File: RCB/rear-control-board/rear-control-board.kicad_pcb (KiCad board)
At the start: 2 copper layers, 99.1 x 99.1 mm, 57 parts, among them J1 Conn_01x23, J2 Conn_01x14, J3 Conn_01x08, J4 Conn_01x02, J5 Conn_01x02, J6 Conn_01x05, K1 T9VV1K15-12S, K2 G5V-2, K3 G5V-2, Q1 BSS84, Q2 2N7002, Q3 Q_PMOS_GDSD, Q4 Q_PMOS_GDSD, Q5 Q_PMOS_GDSD, U1 STM32F413CGUx, U2 LD1117S33TR_SOT223, U3 R-78B5.0-2.0, U4 MCP2551-I-SN, Y1 Crystal

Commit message: DRC and layout update
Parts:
- added G***: LOGO, AERO_Footprints:AERO_Logo_10x4mm, F.Cu at (131.5, 135.3)
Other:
- board text added: "BMS"
- board text added: "DCDC"
- board text added: "G.Spearing 22.032"
- board text added: "HVB"
- board text added: "IMD"
- board text added: "M3 Holes"
- board text added: "Pump"
- board text added: "RCB"
- board text added: "Rinehart"
- board text added: "SSOK"
- board text added: "Spare"

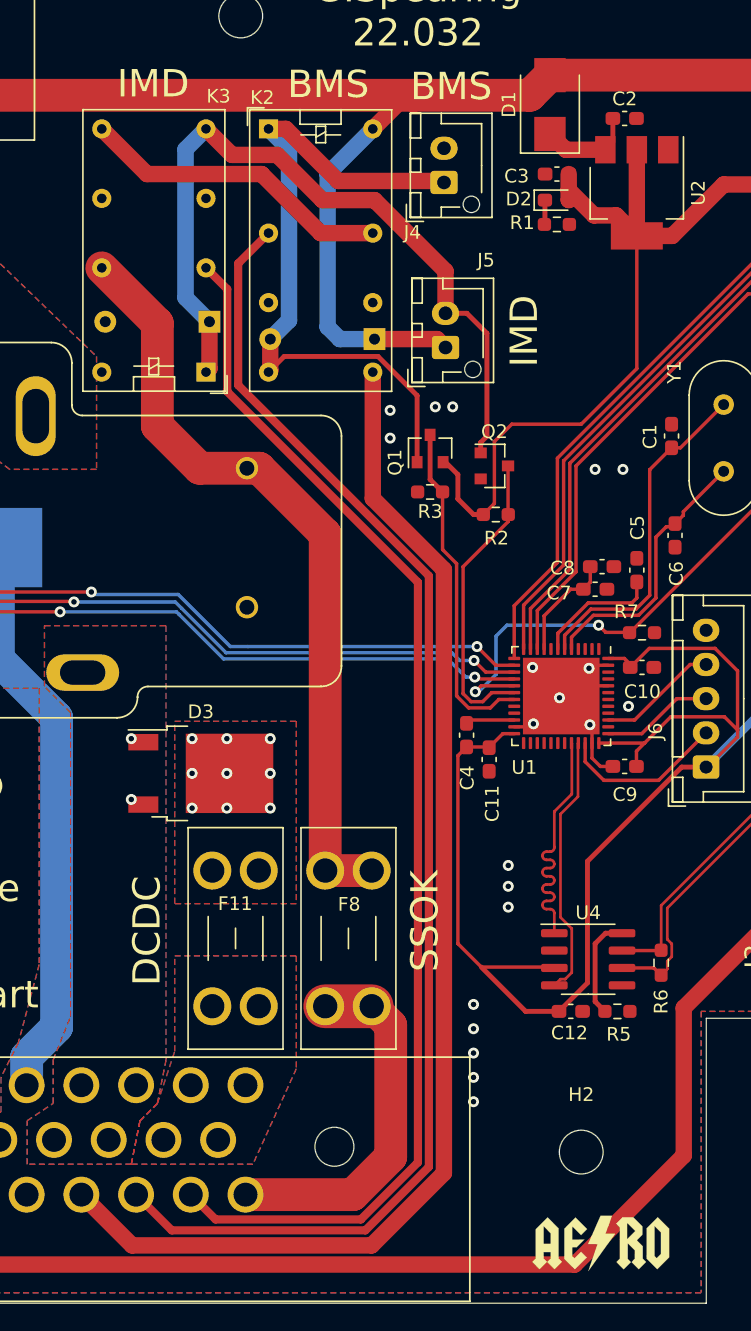
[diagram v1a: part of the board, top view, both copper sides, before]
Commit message: updating footprint and 3d model links
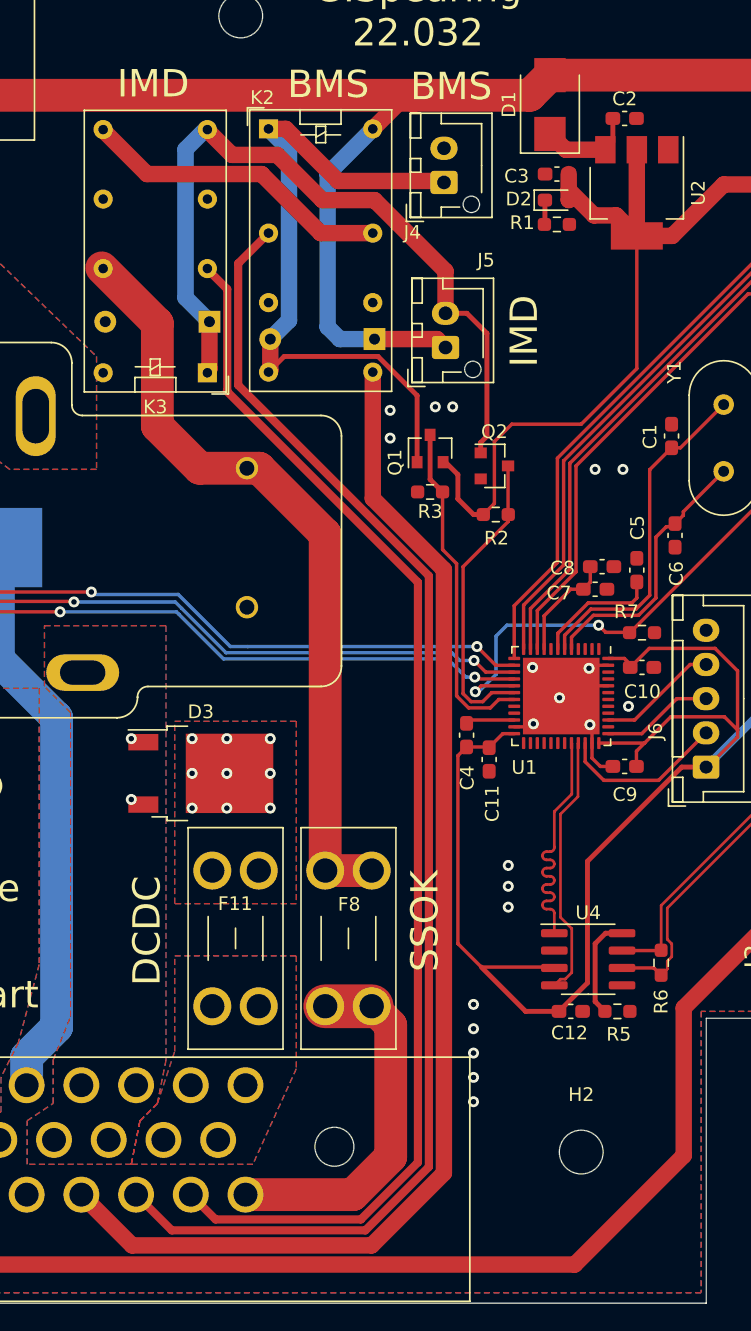
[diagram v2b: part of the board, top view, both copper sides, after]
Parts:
- removed G***: LOGO, AERO_Footprints:AERO_Logo_10x4mm
- moved K3 0.11 mm to (102.7, 71.7)

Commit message: update layout and labeling
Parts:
- moved J2 0.09 mm to (150.9, 58.0)
- moved J1 0.07 mm to (77.5, 123.7)
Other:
- board text added: "3.3V"
- board text added: "CLK"
- board text added: "DIO"
- board text added: "GND"
- board text added: "Trace"

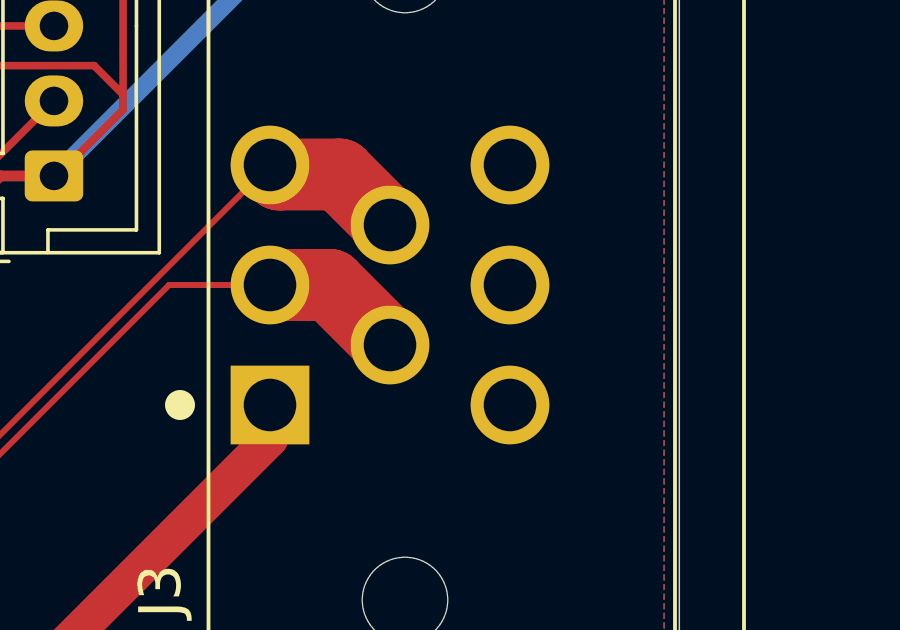
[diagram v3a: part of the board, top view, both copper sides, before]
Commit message: updating can pinouts
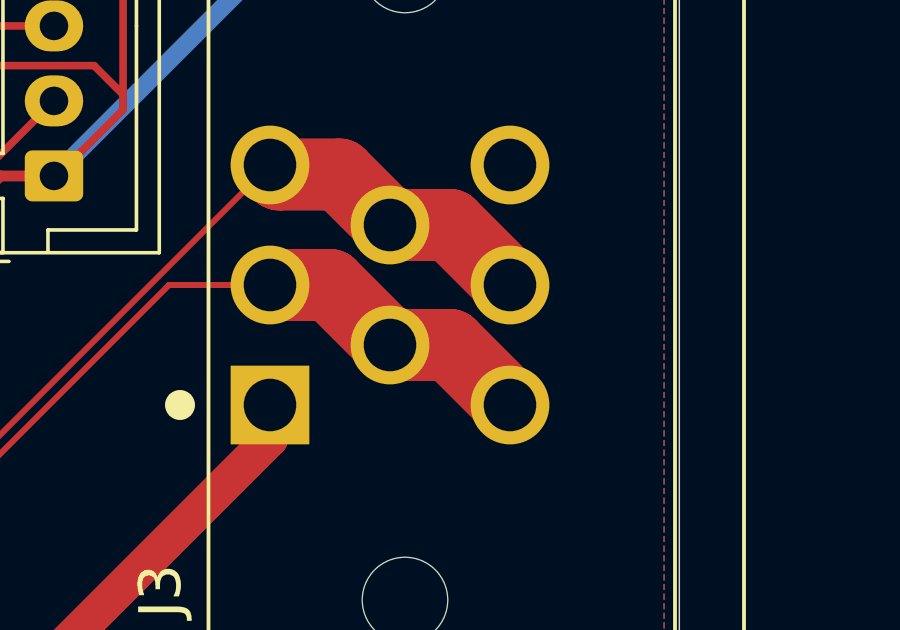
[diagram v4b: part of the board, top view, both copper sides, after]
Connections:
- J3 pad 6: /NC -> /CAN_N
- J3 pad 7: GND -> /CAN_P
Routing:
- net /CAN_P: track 25.8 -> 30.6 mm
- net /CAN_N: track 26.1 -> 30.9 mm

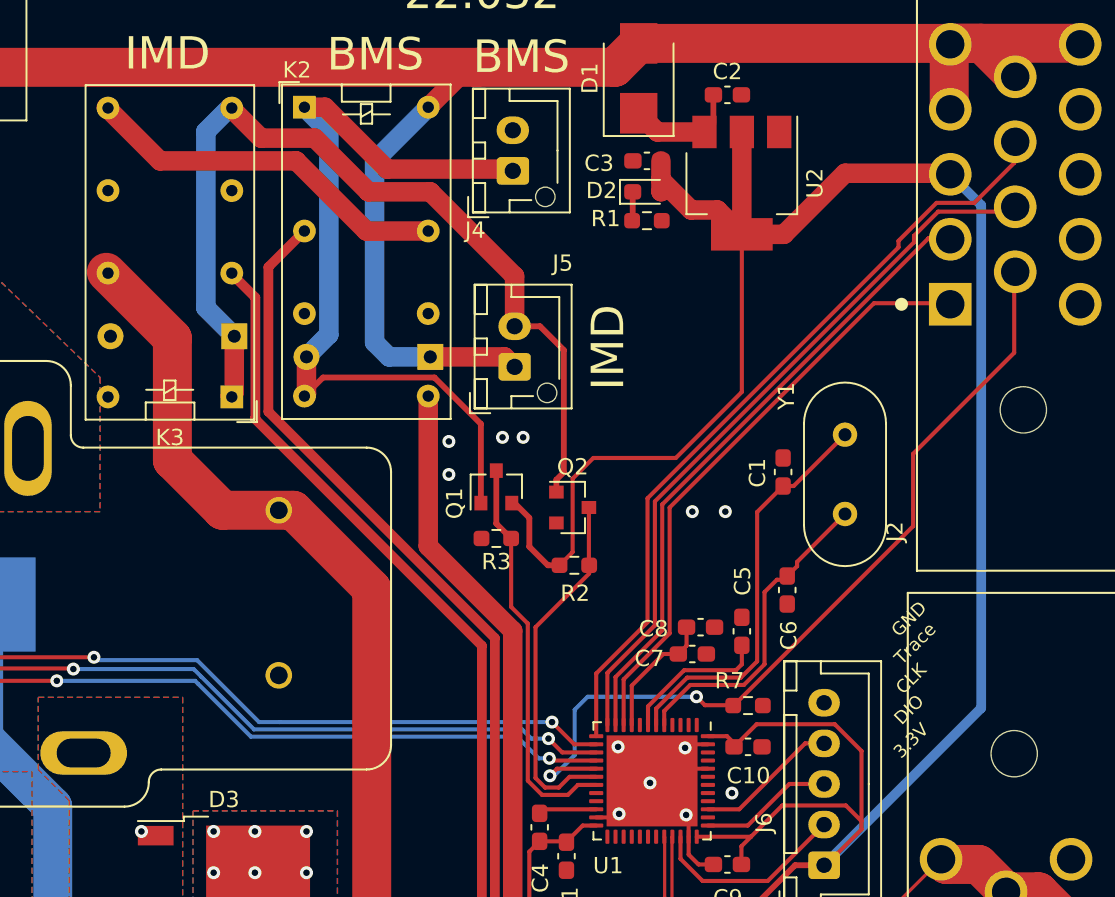
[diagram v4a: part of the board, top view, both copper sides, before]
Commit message: Major Review and Part Update
updating footprints, component values, layouts
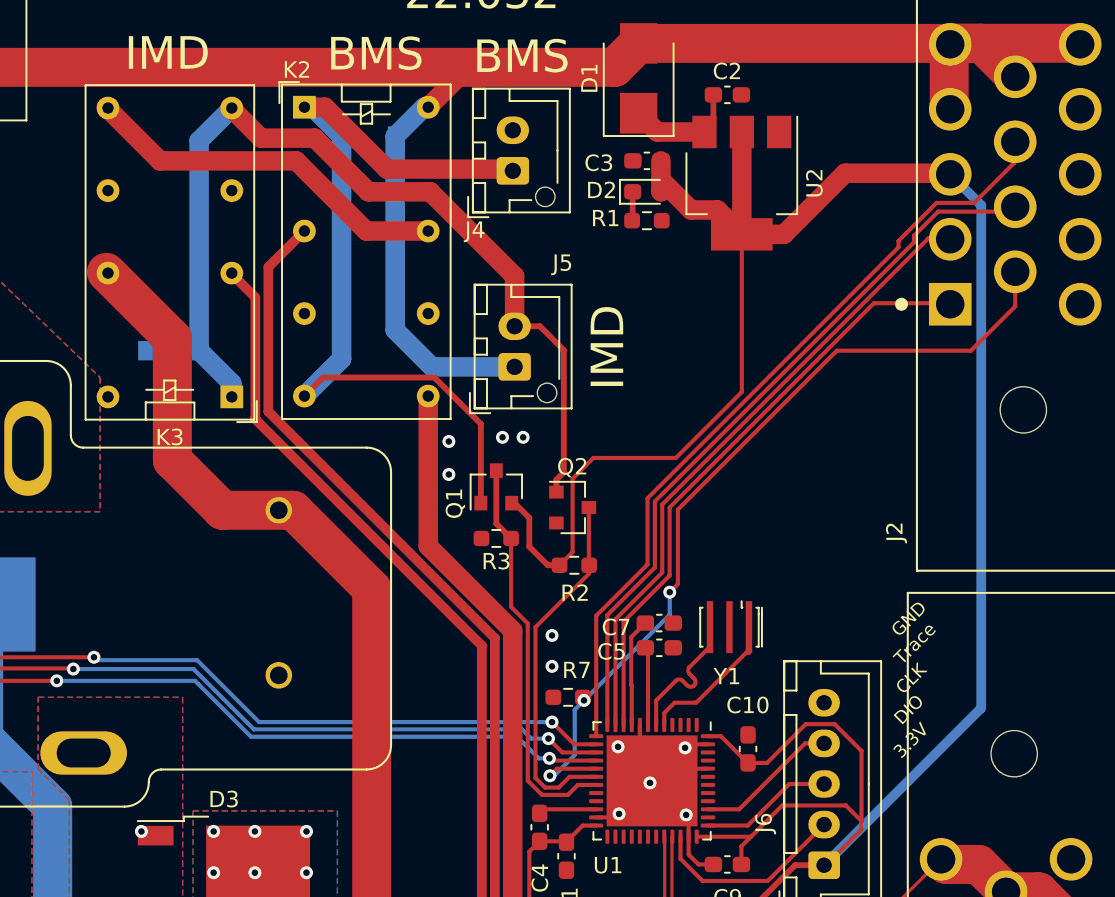
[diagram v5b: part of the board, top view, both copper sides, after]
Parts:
- removed C1, C6: 20p, Capacitor_SMD:C_0603_1608Metric_Pad1.08x0.95mm_HandSolder
- removed C8: 0.1u, Capacitor_SMD:C_0603_1608Metric_Pad1.08x0.95mm_HandSolder
- C13: value C -> 0.1u
- C14: value C -> 10u
- D1: value D_Schottky -> BAT54GW
- D4, D5: footprint Diode_THT:D_DO-35_SOD27_P7.62mm_Horizontal -> Diode_SMD:D_SOD-123
- R1: value 220 -> 330
- Y1: value Crystal -> CSTNE8M00; footprint Crystal:Crystal_HC49-U_Vertical -> AERO_Footprints:Resonator_SMD_muRata_CSTxExxV-3Pin_3.0x1.1mm_HandSoldering
- moved D4 14.1 mm to (111.1, 55.6)
- moved Y1 13.8 mm to (133.3, 85.9), turned to 180 degrees
- moved R7 11.1 mm to (123.4, 90.2), turned to 180 degrees
- moved C5 5.18 mm to (129.0, 87.1), turned to 0 degrees
- moved D5 3.91 mm to (99.1, 68.8)
- moved C7 2.79 mm to (129.0, 85.6)
- moved C10 0.13 mm to (134.5, 93.3), turned to 90 degrees
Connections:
- U1 pad 5: Net-(C6-Pad2) -> Net-(U1-Pad5)
- U1 pad 6: Net-(C1-Pad2) -> Net-(U1-Pad6)
- U1 pad 8: unconnected-(U1-Pad8) -> GND
- Y1 pad 1: Net-(C1-Pad2) -> Net-(U1-Pad5)
- Y1 pad 2: Net-(C6-Pad2) -> GND
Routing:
- net Net-(C1-Pad2): track 25.0 -> 0.00 mm
- net Net-(C6-Pad2): track 19.8 -> 0.00 mm
- net Net-(U1-Pad5): track 0.00 -> 10.6 mm
- net Net-(U1-Pad6): track 0.00 -> 10.3 mm
- net Net-(C5-Pad1): track 9.17 -> 4.82 mm
- net GND: track 19.7 -> 23.5 mm, vias 20 -> 19
- net VDD: track 123.8 -> 121.7 mm
- net Net-(C7-Pad2): track 7.96 -> 6.65 mm
- net /TEMP_WATER-: track 52.1 -> 50.9 mm, vias 2 -> 3
- net /FAULT_LATCHER/bms_switch: track 50.9 -> 51.8 mm
- net +3V3: track 199.1 -> 199.8 mm

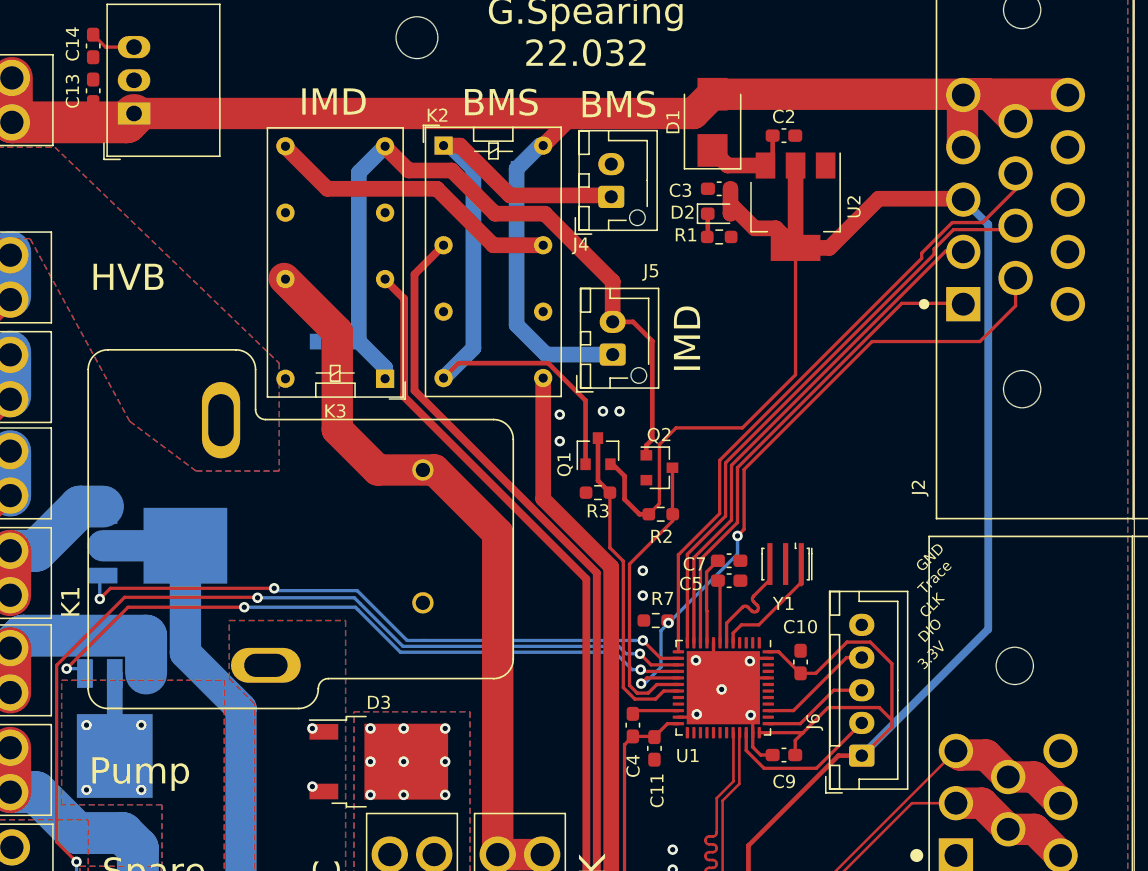
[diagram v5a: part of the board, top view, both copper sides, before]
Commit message: updating pinouts
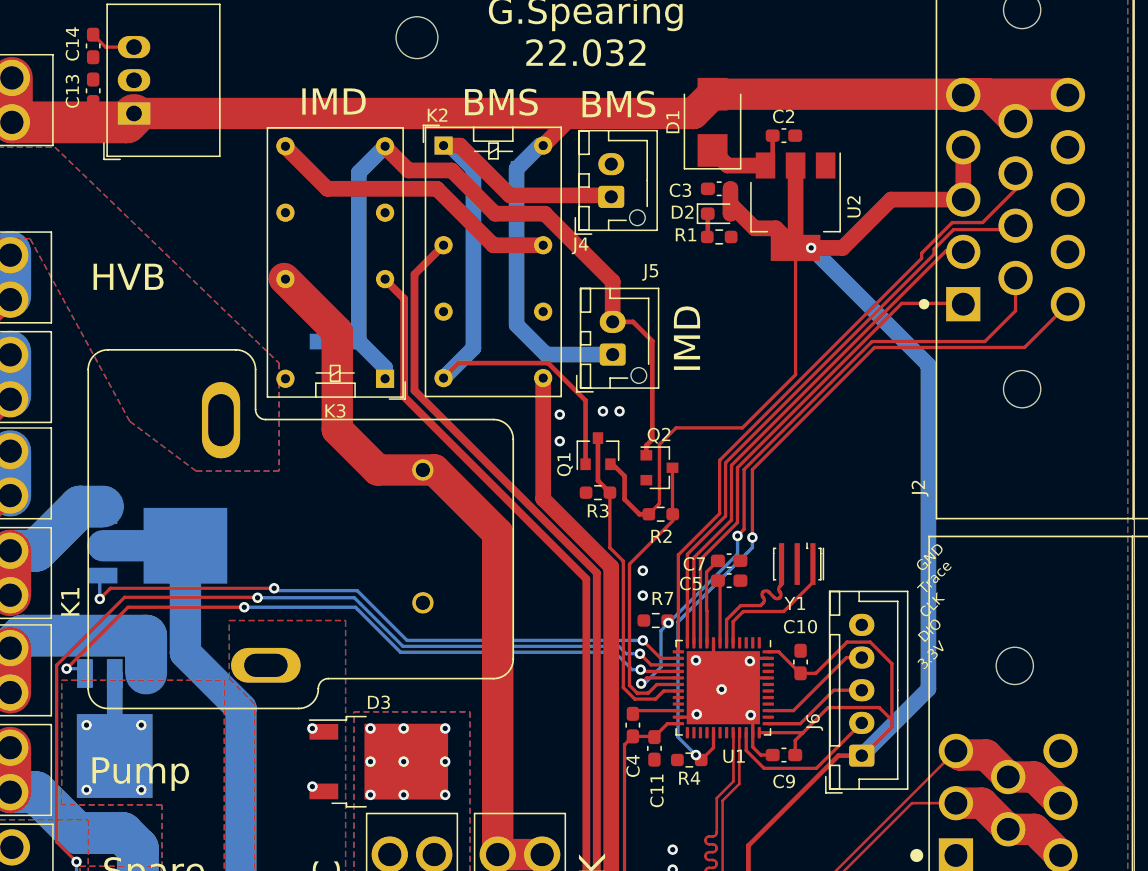
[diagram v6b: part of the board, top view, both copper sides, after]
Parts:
- added R4: 10k, Resistor_SMD:R_0603_1608Metric_Pad0.98x0.95mm_HandSolder, F.Cu at (126.0, 100.8)
- moved Y1 0.89 mm to (134.2, 85.9)
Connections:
- net /TEMP_WATER- renamed /WATER_IN-
- J2 pad 10: GND -> /WATER_OUT-
- J2 pad 4: VDD -> +3V3
- U1 pad 29: unconnected-(U1-Pad29) -> /WATER_OUT-
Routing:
- net /WATER_OUT-: track 0.00 -> 57.2 mm, vias 0 -> 2
- net VDD: track 121.7 -> 117.7 mm
- net +3V3: track 199.8 -> 201.0 mm, vias 0 -> 1
- net /Controller/FAN_CTRL: track 52.3 -> 51.8 mm

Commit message: willem review notes
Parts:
- moved C11 1.70 mm to (122.6, 98.4), turned to 180 degrees
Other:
- board text added: "bring decaps closer can pins on connect doens't need to be big use stm32 standard programming header, 5x10 1.27 pitch -> harwin (the one on the stlink mini) from stm32 go 2.54 then larger (15mil) add via near decoupling pins on caps use 8mil trace minimum check zone spacing, min is 8/8 (thickness/spacing) higher for 12V"
